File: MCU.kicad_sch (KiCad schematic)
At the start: 20 parts, among them SW1 SW_Push, SW2 SW_Push, U1 STM32H750VBTx, Y1 16MHz

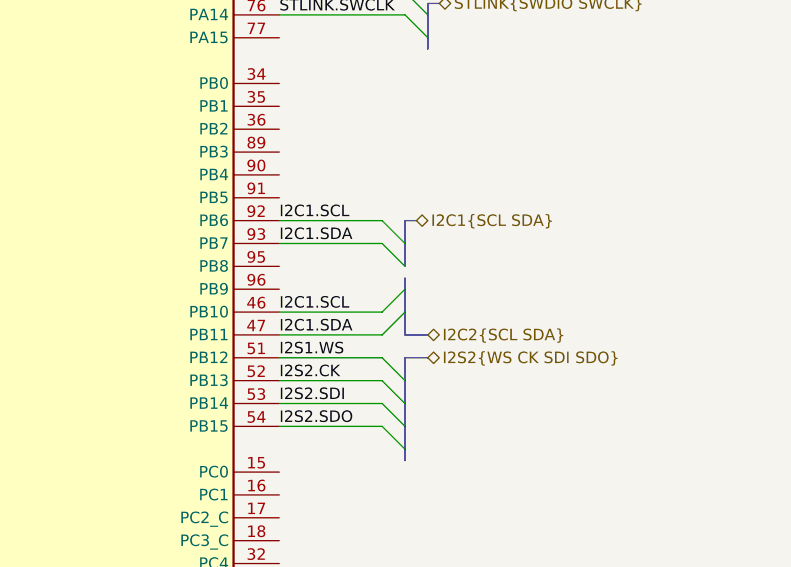
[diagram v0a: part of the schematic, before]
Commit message: MOD : KiCad 8.0.1 -> 9.0.0. ADD : Codec power circuitry.
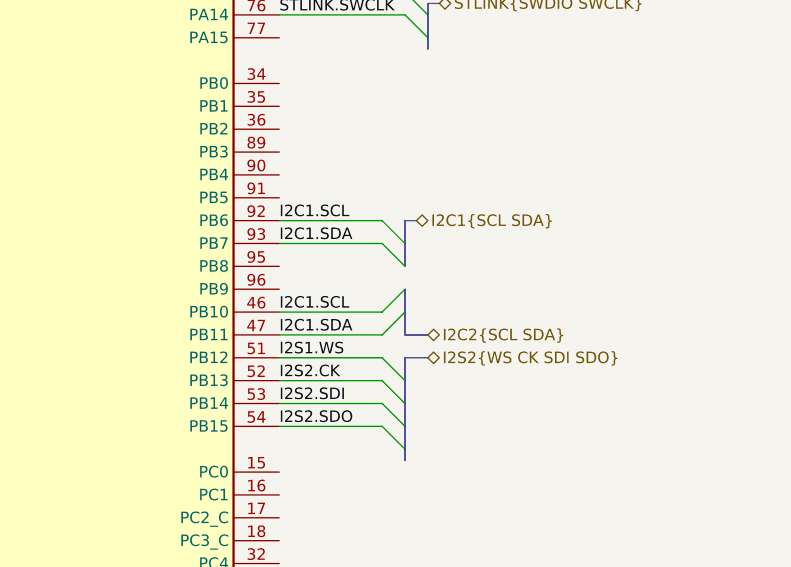
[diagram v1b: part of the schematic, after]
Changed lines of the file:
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@@
 (kicad_sch
-	(version 20231120)
+	(version 20250114)
 	(generator "eeschema")
-	(generator_version "8.0")
+	(generator_version "9.0")
 	(paper "A4")
 	(junction
@@
 		(pts
 			(xy 142.24 173.99) (xy 143.51 173.99)
-		)
-		(stroke
-			(width 0)
-			(type default)
-		)
-	)
-	(bus
-		(pts
-			(xy 179.07 102.87) (xy 179.07 101.6)
 		)
 		(stroke
@@
 		(shape bidirectional)
 		(at 181.61 110.49 0)
-		(fields_autoplaced yes)
 		(effects
 			(font
@@
 		(shape bidirectional)
 		(at 181.61 107.95 0)
-		(fields_autoplaced yes)
 		(effects
 			(font
@@
 		(shape bidirectional)
 		(at 182.88 71.12 0)
-		(fields_autoplaced yes)
 		(effects
 			(font
@@
 		(shape bidirectional)
 		(at 182.88 64.77 0)
-		(fields_autoplaced yes)
 		(effects
 			(font
@@
 		(shape bidirectional)
 		(at 101.6 101.6 180)
-		(fields_autoplaced yes)
 		(effects
 			(font
@@
 		(shape bidirectional)
 		(at 181.61 46.99 0)
-		(fields_autoplaced yes)
 		(effects
 			(font
@@
 		(shape bidirectional)
 		(at 180.34 95.25 0)
-		(fields_autoplaced yes)
 		(effects
 			(font
@@
 		(shape bidirectional)
 		(at 182.88 143.51 0)
-		(fields_autoplaced yes)
-		(effects
-			(font
+		(effects
+			(font

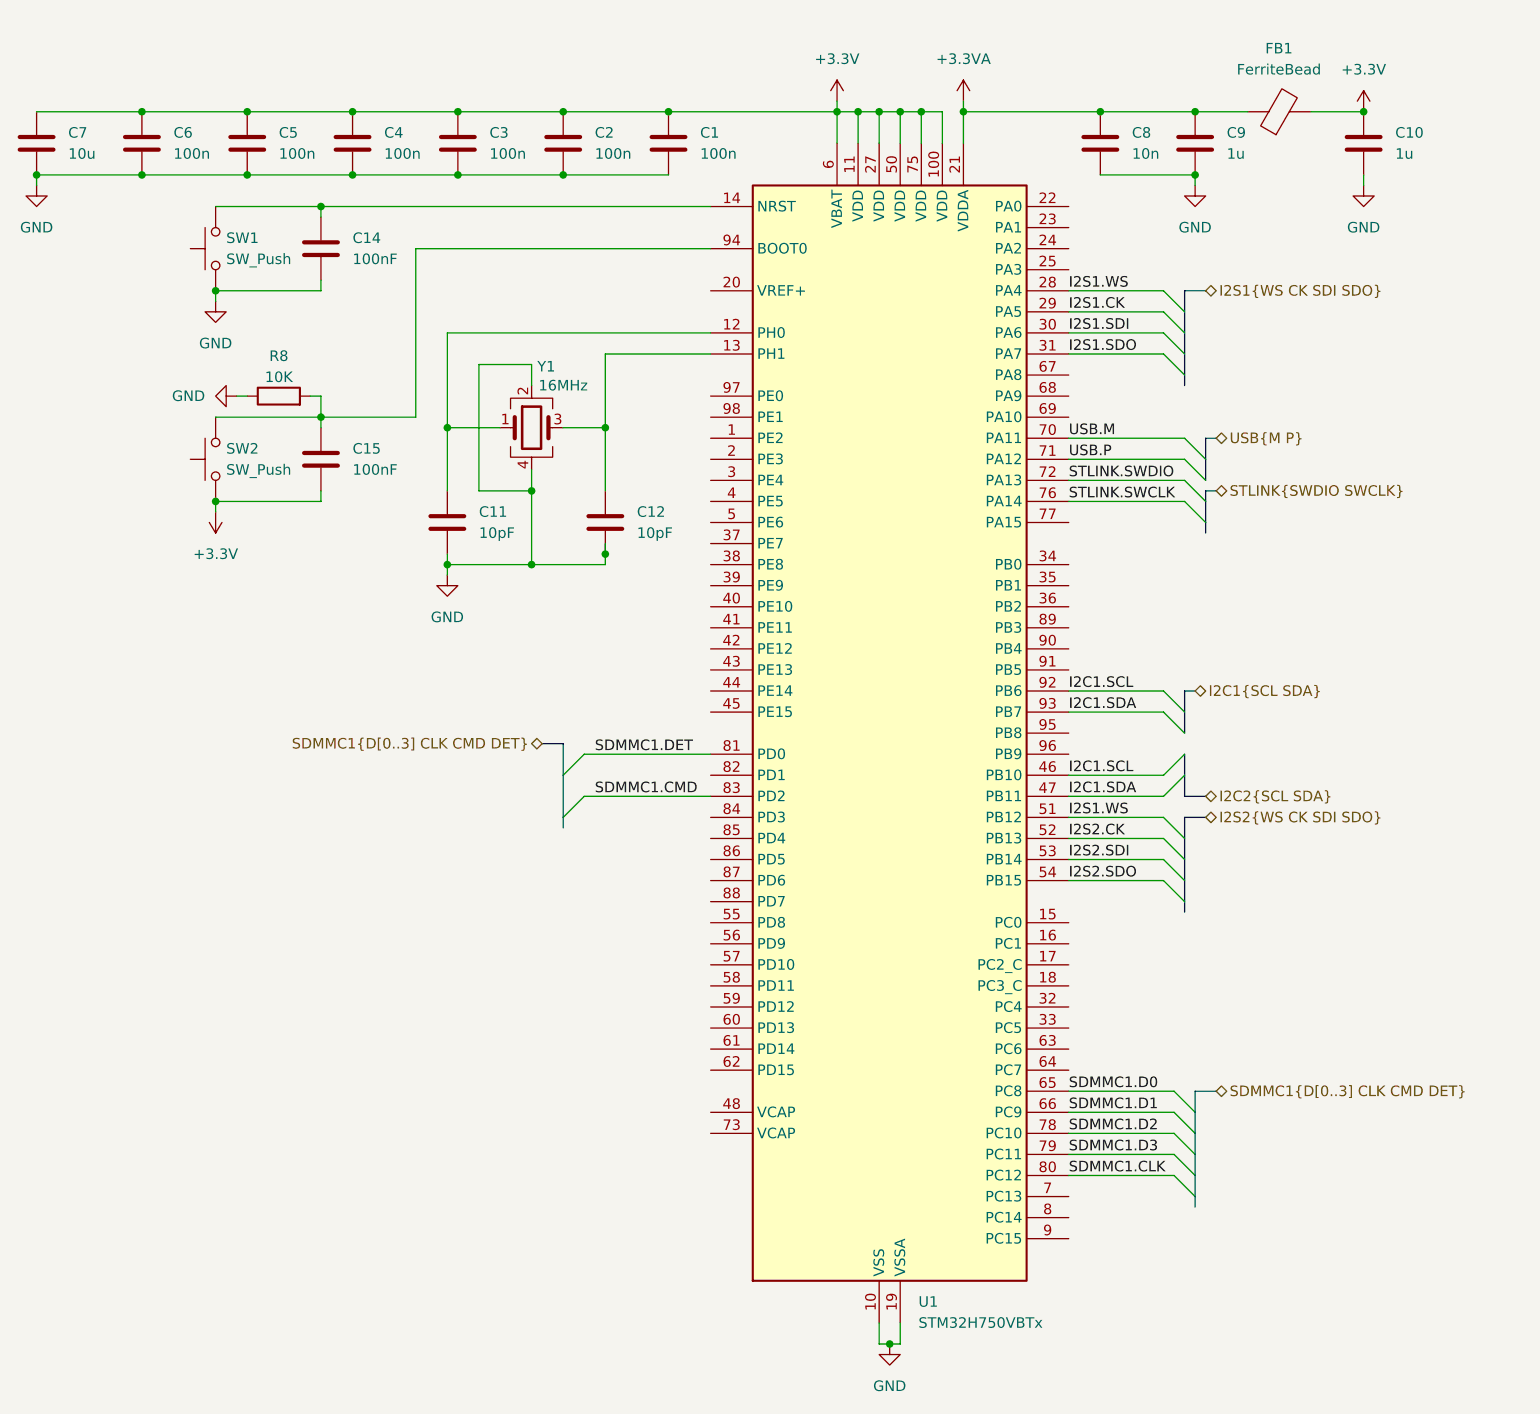
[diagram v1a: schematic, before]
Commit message: ADD : Finished codec power and data connections
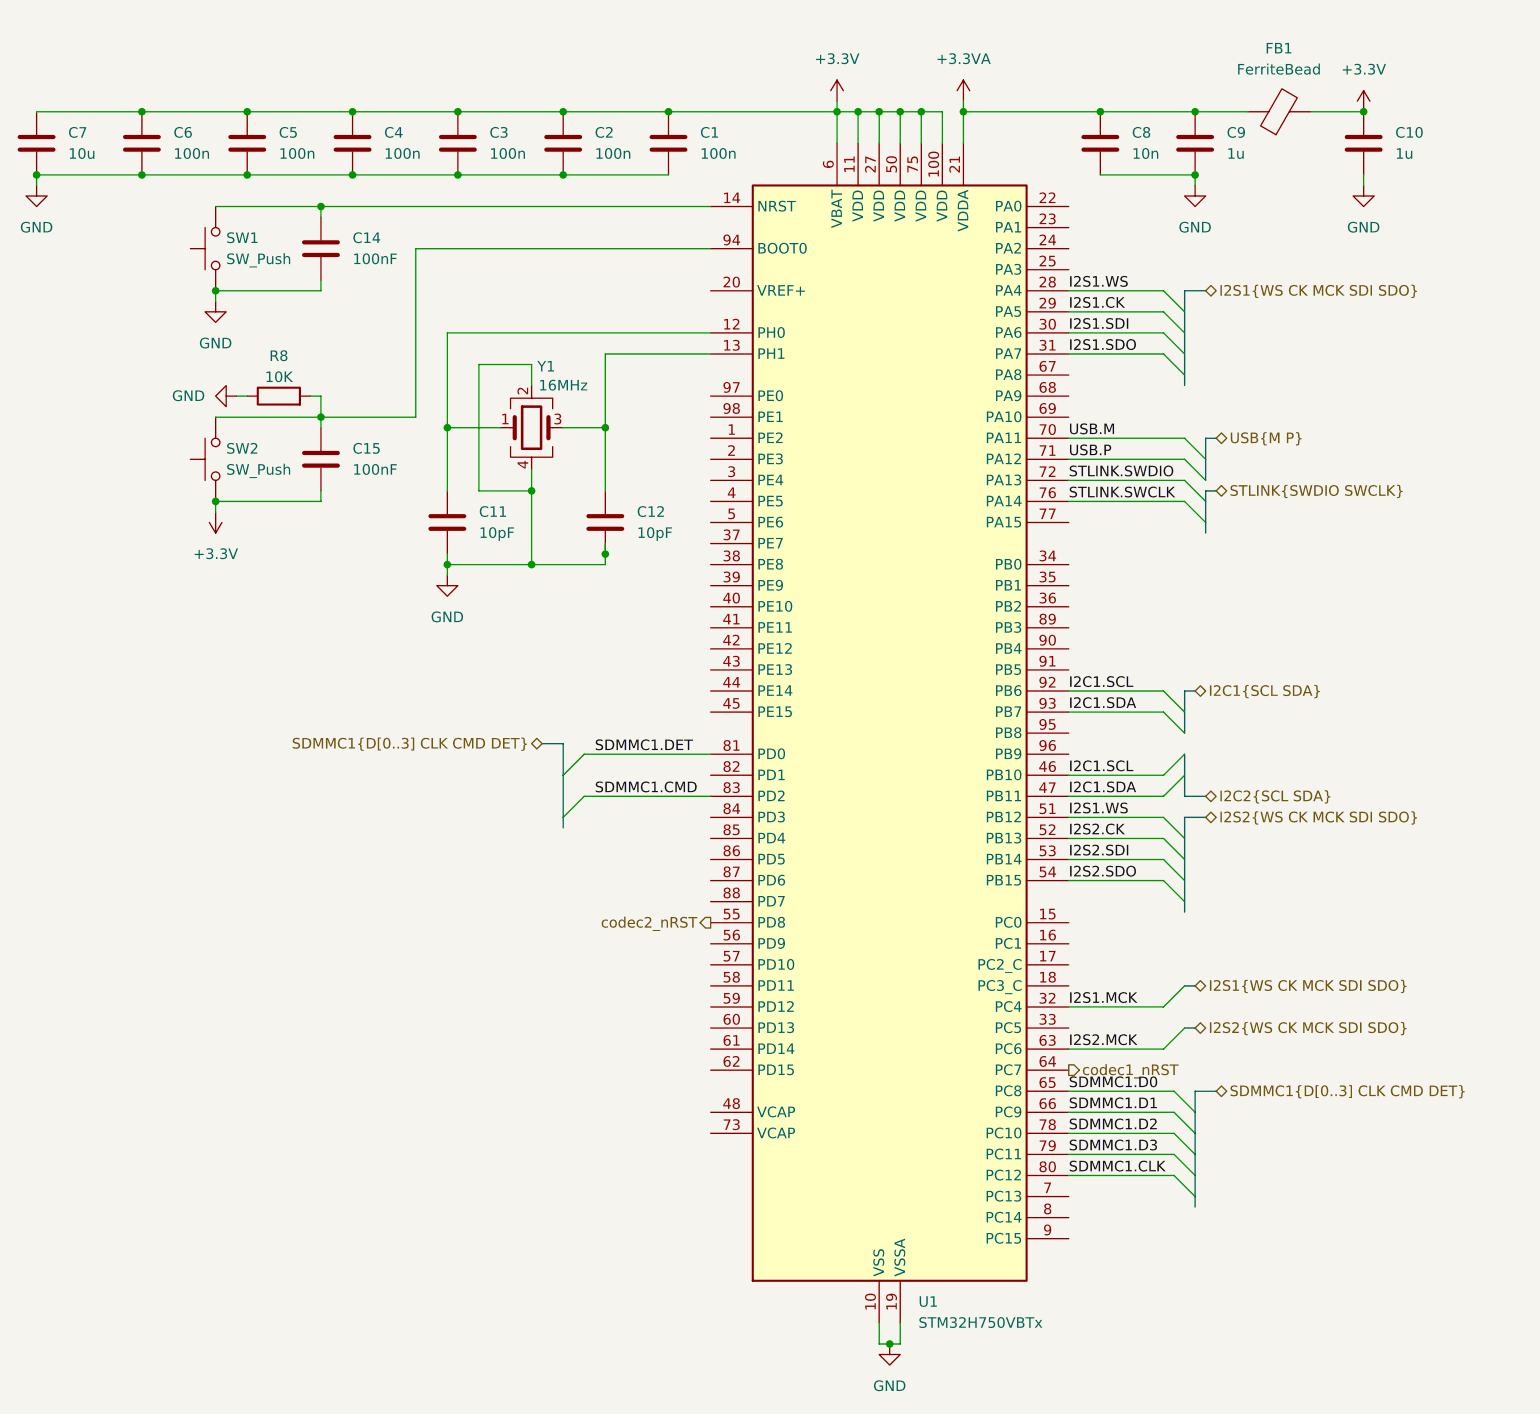
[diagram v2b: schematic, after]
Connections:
- net I2S1.MCK: now reaches U1.32 (PC4)
- net codec2_nRST: now reaches U1.55 (PD8)
- net I2S2.MCK: now reaches U1.63 (PC6)
- net codec1_nRST: now reaches U1.64 (PC7)

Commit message: ADD : Footprint assignment. FIX : Various ERC rules.
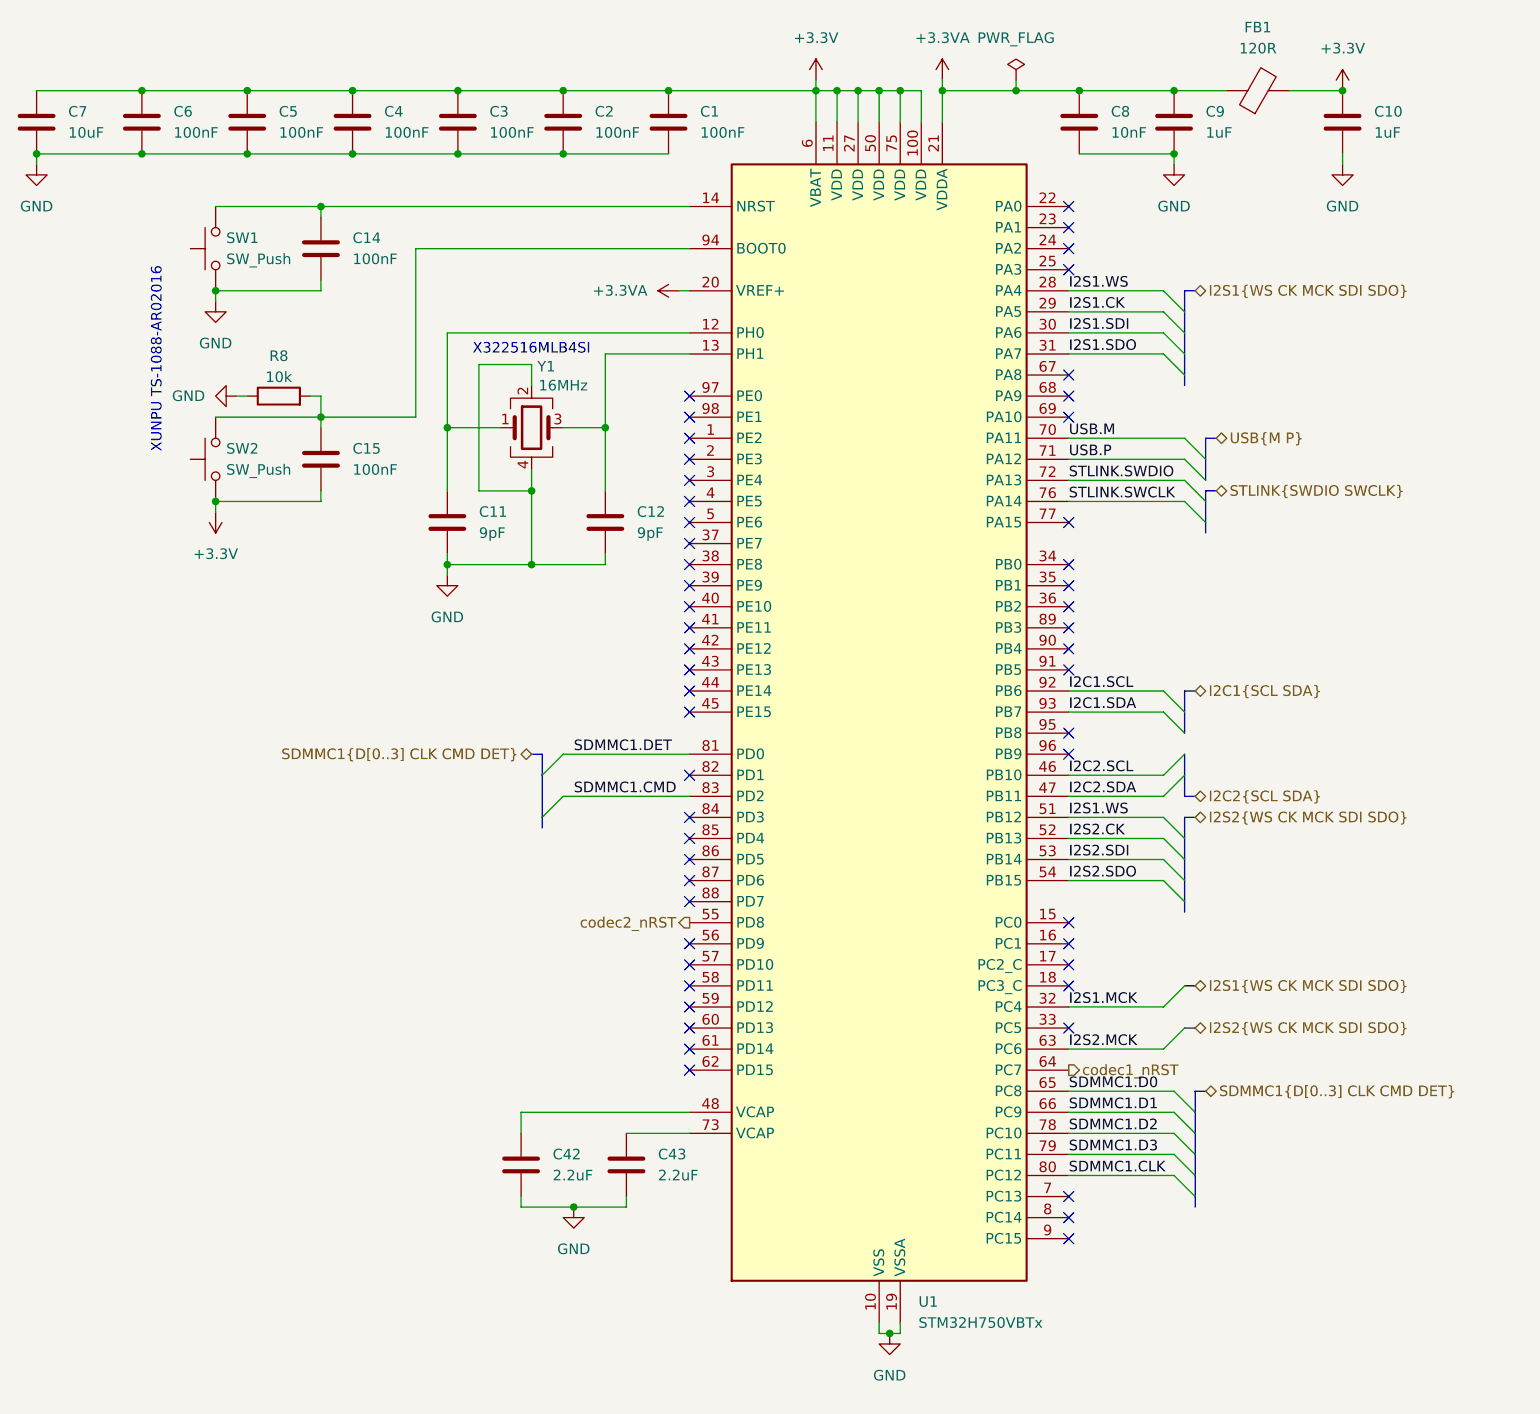
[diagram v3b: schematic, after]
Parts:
- added C42, C43: 2.2uF, Capacitor_SMD:C_0402_1005Metric, symbol Device:C
- C1, C2, C3, C4, C5, C6: value 100n -> 100nF; footprint (none) -> Capacitor_SMD:C_0402_1005Metric
- C10, C9: value 1u -> 1uF; footprint (none) -> Capacitor_SMD:C_0402_1005Metric
- C11, C12: value 10pF -> 9pF; footprint (none) -> Capacitor_SMD:C_0402_1005Metric
- C14, C15: footprint (none) -> Capacitor_SMD:C_0402_1005Metric
- C7: value 10u -> 10uF; footprint (none) -> Capacitor_SMD:C_0402_1005Metric
- C8: value 10n -> 10nF; footprint (none) -> Capacitor_SMD:C_0402_1005Metric
- FB1: value FerriteBead -> 120R; footprint (none) -> Resistor_SMD:R_0402_1005Metric
- R8: value 10K -> 10k; footprint (none) -> Resistor_SMD:R_0402_1005Metric
- SW1, SW2: footprint (none) -> random-footprints:SW_TS-1088-AR02016
- Y1: footprint (none) -> Crystal:Crystal_SMD_3225-4Pin_3.2x2.5mm
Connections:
- net +3.3VA: now also U1.20 (VREF+)
- net GND: now also C42.2, C43.2
- net I2C1.SCL: no longer U1.46 (PB10)
- net I2C1.SDA: no longer U1.47 (PB11)
- net at U1.48 (VCAP): now also C42.1
- net at U1.73 (VCAP): now also C43.1
- new net I2C2.SCL: U1.46 (PB10)
- new net I2C2.SDA: U1.47 (PB11)
- no-connect marks 0 -> 53
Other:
- note added: "X322516MLB4SI"
- note added: "XUNPU TS-1088-AR02016"
- moved on the sheet: C1, C10, C2, C3, C4, C5, C6, C7, C8, C9, FB1, U1
